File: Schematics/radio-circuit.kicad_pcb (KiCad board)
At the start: 4 copper layers, 59 x 29.5 mm, 36 parts, among them J2 STDC14, J3 0, J4 USB_A, U1 USBLC6-2SC6, U2 LD39015M33R, U3 STM32F042F6Px, U4 Si4705-D60-GM, Y1 SG-3030CM

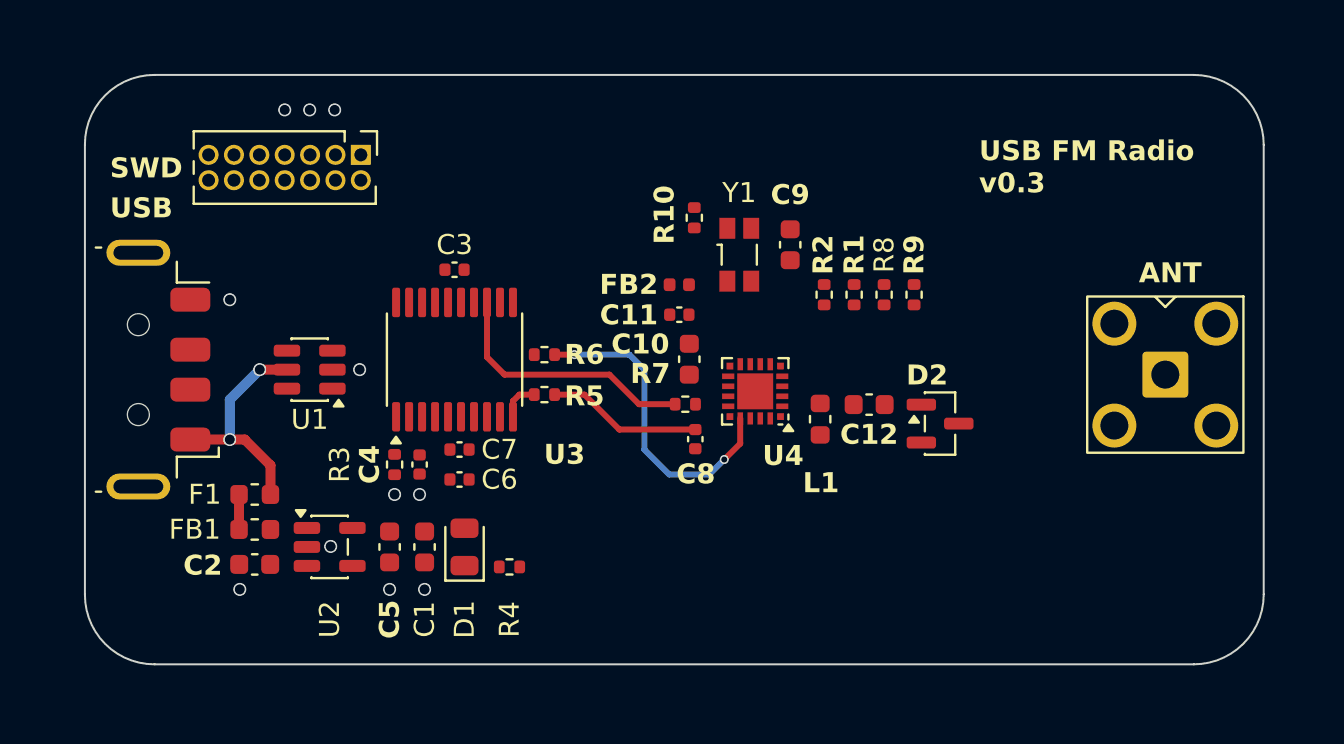
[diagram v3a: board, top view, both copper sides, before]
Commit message: Switched radio GPIOs to the same side, and updated some labels
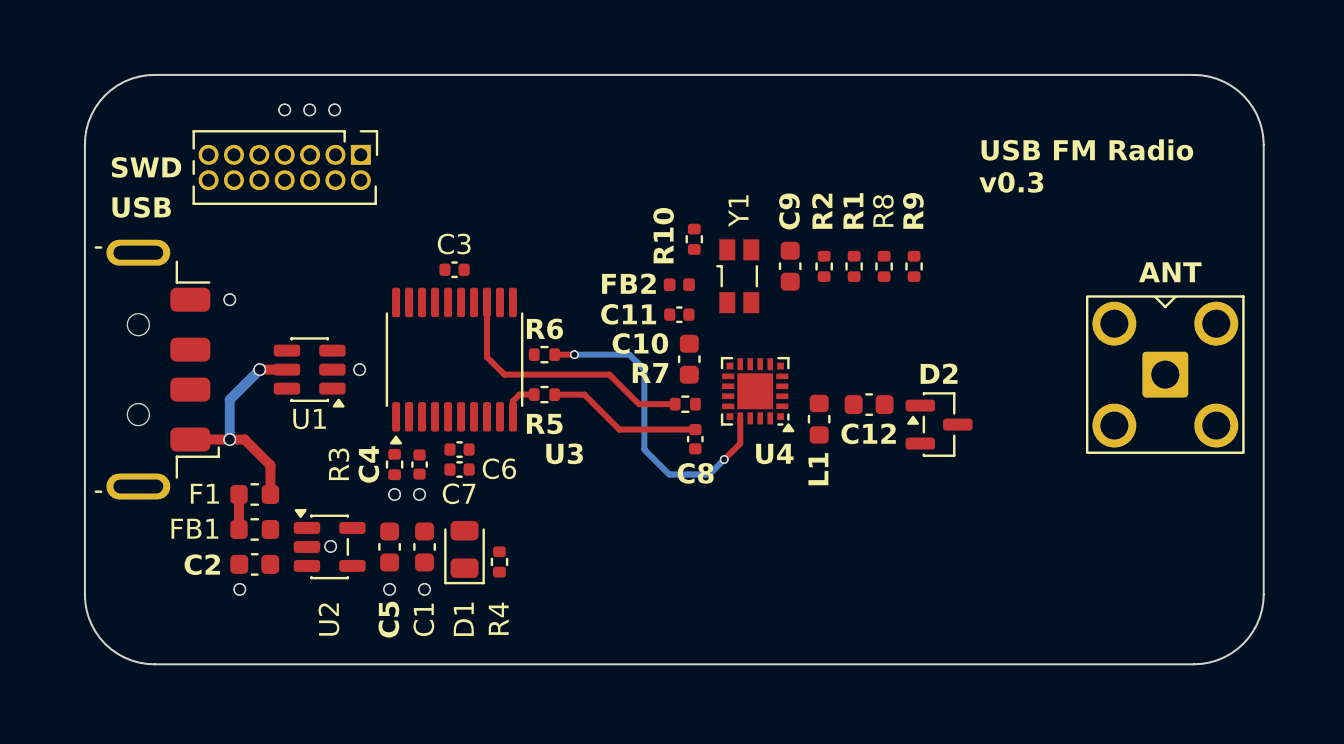
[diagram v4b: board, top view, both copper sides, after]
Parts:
- moved R1 1.42 mm to (200.5, 119.6)
- moved R2 1.42 mm to (199.0, 119.6)
- moved R8 1.42 mm to (202.0, 119.6)
- moved R9 1.42 mm to (203.5, 119.6)
- moved C9 1.08 mm to (197.3, 119.6)
- moved Y1 1.08 mm to (194.8, 120.1)
- moved R10 1.07 mm to (192.5, 118.2)
- moved R4 0.56 mm to (182.8, 134.4), turned to 90 degrees
- moved C6 0.50 mm to (180.8, 129.8)
- moved D1 0.12 mm to (181.0, 133.8)
- moved D2 0.07 mm to (204.8, 127.5)
- moved L1 0.05 mm to (198.8, 127.2)
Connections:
- U3 pad 14: ~{RD_RST} -> unconnected-(U3-PB1-Pad14)
- U3 pad 7: unconnected-(U3-PA1-Pad7) -> ~{RD_RST}
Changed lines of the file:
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@@
 		(capping no)
 		(filling no)
-		(zone_defaults)
 		(pcbplotparams
 			(layerselection 0x00000000_00000000_55555555_5755f5ff)
@@
 	(footprint "Capacitor_SMD:C_0402_1005Metric"
 		(layer "F.Cu")
-		(at 180.75 130.25)
+		(at 180.75 129.75)
 		(descr "Capacitor SMD 0402 (1005 Metric), square (rectangular) end terminal, IPC-7351 nominal, (Body size source: IPC-SM-782 page 76, https://www.pcb-3d.com/wordpress/wp-content/uploads/ipc-sm-782a_amendment_1_and_2.pdf)")
 		(tags "capacitor")
@@
 	(footprint "Package_TO_SOT_SMD:SOT-23"
 		(layer "F.Cu")
-		(at 204.8 127.45)
+		(at 204.75 127.5)
 		(descr "SOT, 3 Pin (JEDEC TO-236 Var AB https://www.jedec.org/document_search?search_api_views_fulltext=TO-236)")
 		(tags "SOT TO_SOT_SMD")
 		(property "Reference" "D2"
-			(at -0.65 -2.42 0)
+			(at 0 -2.5 180)
 			(layer "F.SilkS")
 			(effects
@@
 			(layers "F.Cu" "F.Mask" "F.Paste")
 			(roundrect_rratio 0.25)
-			(net "unconnected-(U3-PA1-Pad7)")
+			(net "~{RD_RST}")
 			(pinfunction "PA1_7")
-			(pintype "bidirectional+no_connect")
+			(pintype "bidirectional")
 		)
 		(pad "8" smd roundrect
@@
 			(layers "F.Cu" "F.Mask" "F.Paste")
 			(roundrect_rratio 0.25)
-			(net "~{RD_RST}")
+			(net "unconnected-(U3-PB1-Pad14)")
 			(pinfunction "PB1_14")
-			(pintype "bidirectional")
+			(pintype "bidirectional+no_connect")
 		)
 		(pad "15" smd roundrect
@@
 		(tags "capacitor")
 		(property "Reference" "C12"
-			(at 0 -1.5 0)
+			(at 0 -1.5 180)
 			(layer "F.SilkS")
 			(effects
@@
 	(footprint "Resistor_SMD:R_0402_1005Metric"
 		(layer "F.Cu")
-		(at 192.5 117.15 90)
+		(at 192.5 118.225 90)
 		(descr "Resistor SMD 0402 (1005 Metric), square (rectangular) end terminal, IPC-7351 nominal, (Body size source: IPC-SM-782 page 72, https://www.pcb-3d.com/wordpress/wp-content/uploads/ipc-sm-782a_amendment_1_and_2.pdf)")
 		(tags "resistor")
@@
 	(footprint "Capacitor_SMD:C_0603_1608Metric"
 		(layer "F.Cu")
-		(at 197.3 118.5 -90)
+		(at 197.3 119.575 -90)
 		(descr "Capacitor SMD 0603 (1608 Metric), square (rectangular) end terminal, IPC-7351 nominal, (Body size source: IPC-SM-782 page 76, https://www.pcb-3d.com/wordpress/wp-content/uploads/ipc-sm-782a_amendment_1_and_2.pdf)")
 		(tags "capacitor")
 		(property "Reference" "C9"
-			(at -2.5 0 0)
+			(at -2.75 0 90)
 			(layer "F.SilkS")
 			(effects
@@
 	(footprint "Resistor_SMD:R_0402_1005Metric"
 		(layer "F.Cu")
-		(at 200.5 121 -90)
+		(at 200.5 119.585 -90)
 		(descr "Resistor SMD 0402 (1005 Metric), square (rectangular) end terminal, IPC-7351 nominal, (Body size source: IPC-SM-782 page 72, https://www.pcb-3d.com/wordpress/wp-content/uploads/ipc-sm-782a_amendment_1_and_2.pdf)")
 		(tags "resistor")
 		(property "Reference" "R1"
-			(at -2 0 90)
+			(at -2.76 0 90)
 			(layer "F.SilkS")
 			(effects
@@
 	(footprint "Inductor_SMD:L_0603_1608Metric"
 		(layer "F.Cu")
-		(at 198.8 127.23 90)
+		(at 198.75 127.23 90)
 		(descr "Inductor SMD 0603 (1608 Metric), square (rectangular) end terminal, IPC-7351 nominal, (Body size source: http://www.tortai-tech.com/upload/download/2011102023233369053.pdf)")
 		(tags "inductor")
 		(property "Reference" "L1"
-			(at -3.19 0.04 180)
+			(at -2.52 0 270)
 			(layer "F.SilkS")
 			(effects
@@
 		(tags "resistor")
 		(property "Reference" "R5"
-			(at 2 0.075 0)
+			(at 0 1.5 0)
 			(layer "F.SilkS")
 			(effects
@@
 		(tags "capacitor")
 		(property "Reference" "C7"
-			(at 2 0 0)
+			(at 0 2.25 0)
 			(layer "F.SilkS")
 			(effects
@@
 	(footprint "Oscillator:Oscillator_SMD_SeikoEpson_SG3030CM"
 		(layer "F.Cu")
-		(at 194.75 119 -90)
+		(at 194.75 120.075 -90)
 		(descr "SMD Crystal Oscillator Seiko Epson SG-3030CM package")
 		(tags "SMD SMT crystal oscillator")
 		(property "Reference" "Y1"
-			(at -3.1 0 180)
+			(at -3.325 0 270)
 			(layer "F.SilkS")
 			(effects
@@
 	(footprint "Resistor_SMD:R_0402_1005Metric"
 		(layer "F.Cu")
-		(at 199 121 -90)
+		(at 199 119.585 -90)
 		(descr "Resistor SMD 0402 (1005 Metric), square (rectangular) end terminal, IPC-7351 nominal, (Body size source: IPC-SM-782 page 72, https://www.pcb-3d.com/wordpress/wp-content/uploads/ipc-sm-782a_amendment_1_and_2.pdf)")
 		(tags "resistor")
 		(property "Reference" "R2"
-			(at -2 0.05 270)
+			(at -2.76 0.05 270)
 			(layer "F.SilkS")
 			(effects
@@
 		(tags "resistor")
 		(property "Reference" "R6"
-			(at 2 0 180)
+			(at 0 -1.25 180)
 			(layer "F.SilkS")
 			(effects
@@
 	(footprint "LED_SMD:LED_0805_2012Metric"
 		(layer "F.Cu")
-		(at 181 133.625 90)
+		(at 181 133.75 90)
 		(descr "LED SMD 0805 (2012 Metric), square (rectangular) end terminal, IPC-7351 nominal, (Body size source: https://docs.google.com/spreadsheets/d/1BsfQQcO9C6DZCsRaXUlFlo91Tg2WpOkGARC1WS5S8t0/edit?usp=sharing)")
 		(tags "LED")
 		(property "Reference" "D1"
-			(at -3.625 0 90)
+			(at -3.5 0 90)
 			(layer "F.SilkS")
 			(effects
@@
 	(footprint "Resistor_SMD:R_0402_1005Metric"
 		(layer "F.Cu")
-		(at 202 121 -90)
+		(at 202 119.585 -90)
 		(descr "Resistor SMD 0402 (1005 Metric), square (rectangular) end terminal, IPC-7351 nominal, (Body size source: IPC-SM-782 page 72, https://www.pcb-3d.com/wordpress/wp-content/uploads/ipc-sm-782a_amendment_1_and_2.pdf)")
 		(tags "resistor")
 		(property "Reference" "R8"
-			(at -2 0 90)
+			(at -2.76 0 90)
 			(layer "F.SilkS")
 			(effects
@@
 	(footprint "Resistor_SMD:R_0402_1005Metric"
 		(layer "F.Cu")
-		(at 203.5 121 -90)
+		(at 203.5 119.585 -90)
 		(descr "Resistor SMD 0402 (1005 Metric), square (rectangular) end terminal, IPC-7351 nominal, (Body size source: IPC-SM-782 page 72, https://www.pcb-3d.com/wordpress/wp-content/uploads/ipc-sm-782a_amendment_1_and_2.pdf)")
 		(tags "resistor")
 		(property "Reference" "R9"
-			(at -2 0 90)
+			(at -2.76 0 90)
 			(layer "F.SilkS")
 			(effects
@@
 	(footprint "Resistor_SMD:R_0402_1005Metric"
 		(layer "F.Cu")
-		(at 183.25 134.625)
+		(at 182.75 134.375 90)
 		(descr "Resistor SMD 0402 (1005 Metric), square (rectangular) end terminal, IPC-7351 nominal, (Body size source: IPC-SM-782 page 72, https://www.pcb-3d.com/wordpress/wp-content/uploads/ipc-sm-782a_amendment_1_and_2.pdf)")
 		(tags "resistor")
 		(property "Reference" "R4"
-			(at 0 2.625 90)
+			(at -2.875 0 90)
 			(layer "F.SilkS")
 			(effects
@@
 		)
 		(property "Value" "1k5"
-			(at 0 1.17 0)
+			(at 0 1.17 90)
 			(layer "F.Fab")
 			(effects
@@
 		)
 		(property "Datasheet" ""
-			(at 0 0 0)
+			(at 0 0 90)
 			(layer "F.Fab")
 			(hide yes)
@@
 		)
 		(property "Description" "Resistor"
-			(at 0 0 0)
+			(at 0 0 90)
 			(layer "F.Fab")
 			(hide yes)
@@
 		)
 		(property "Sim.Library" ""
-			(at 0 0 0)
+			(at 0 0 90)
 			(unlocked yes)
 			(layer "F.Fab")
@@
 		)
 		(property "Sim.Name" ""
-			(at 0 0 0)
+			(at 0 0 90)
 			(unlocked yes)
 			(layer "F.Fab")
@@
 		)
 		(property "JLCPCB Part Number" "C25867"
-			(at 0 0 0)
+			(at 0 0 90)
 			(unlocked yes)
 			(layer "F.Fab")
@@
 		)
 		(fp_text user "${REFERENCE}"
-			(at 0 0 0)
+			(at 0 0 90)
 			(layer "F.Fab")
 			(effects
@@
 		)
 		(pad "1" smd roundrect
-			(at -0.51 0)
+			(at -0.51 0 90)
 			(size 0.54 0.64)
 			(layers "F.Cu" "F.Mask" "F.Paste")
@@
 		)
 		(pad "2" smd roundrect
-			(at 0.51 0)
+			(at 0.51 0 90)
 			(size 0.54 0.64)
 			(layers "F.Cu" "F.Mask" "F.Paste")
@@
 		(tags "QFN 0.5")
 		(property "Reference" "U4"
-			(at -1.395 -3.225 180)
+			(at -0.95 -3.165 180)
 			(layer "F.SilkS")
 			(effects
